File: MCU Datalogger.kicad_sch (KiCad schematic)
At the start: 25 parts, among them U1 24LC1025, U2 24LC1025, U3 ATMEGA328P-AU, U4 DS1337S_, Y1 Crystal, Y2 Crystal

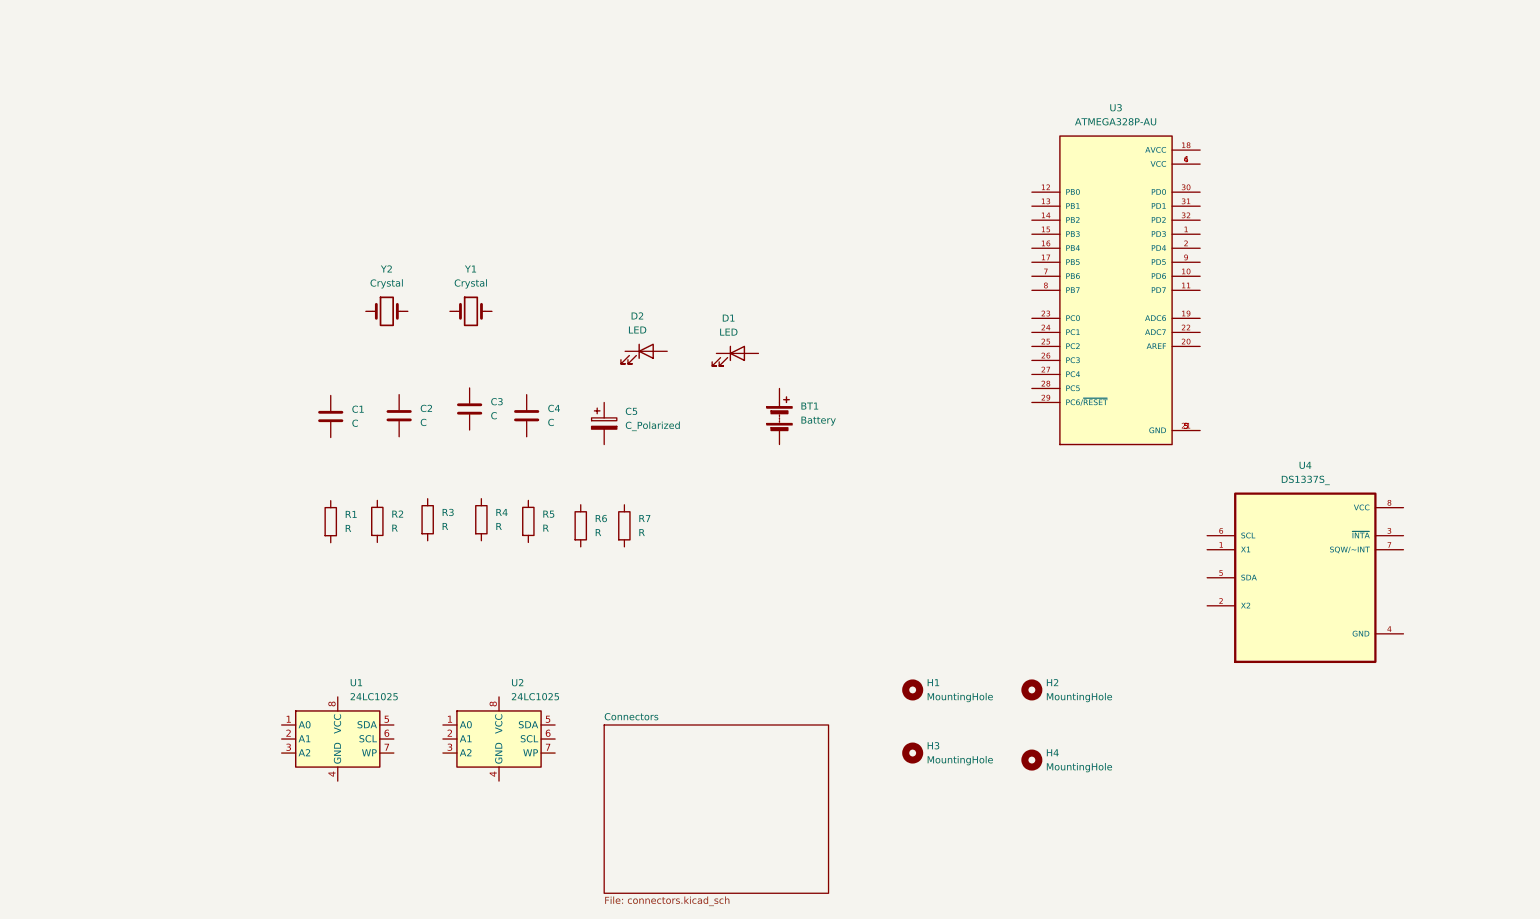
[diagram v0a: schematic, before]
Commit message: assigned footprint libraries
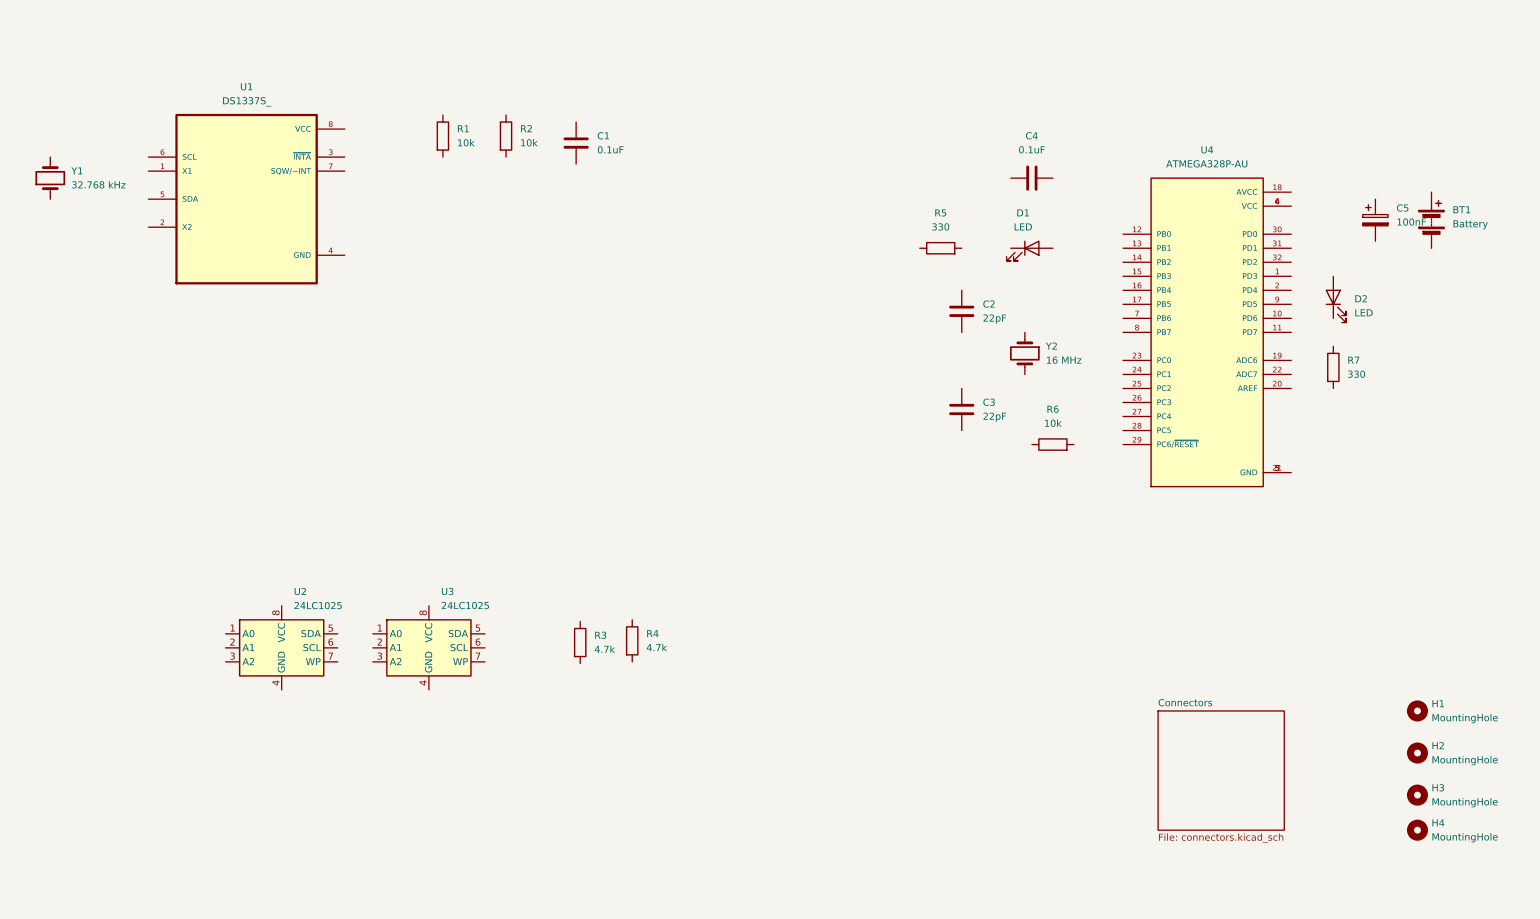
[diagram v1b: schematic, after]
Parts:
- removed U1: 24LC1025, symbol Memory_EEPROM:24LC1025
- removed U3: ATMEGA328P-AU, ATMEGA328P-AU:QFP80P900X900X120-32N, symbol ATMEGA328P-AU:ATMEGA328P-AU
- removed U4: DS1337S_, DS1337S_:SOIC127P600X175-8N, symbol DS1337S_:DS1337S_
- added U1: DS1337S_, footprints:SOIC127P600X175-8N, symbol DS1337S_:DS1337S_
- added U3: 24LC1025, Package_SO:SOIC-8_5.23x5.23mm_P1.27mm, symbol Memory_EEPROM:24LC1025
- added U4: ATMEGA328P-AU, footprints:QFP80P900X900X120-32N, symbol ATMEGA328P-AU:ATMEGA328P-AU
- BT1: footprint (none) -> Connector_PinHeader_2.54mm:PinHeader_1x02_P2.54mm_Vertical
- C1, C4: value C -> 0.1uF; footprint (none) -> Capacitor_SMD:C_0805_2012Metric
- C2, C3: value C -> 22pF; footprint (none) -> Capacitor_SMD:C_0805_2012Metric
- C5: value C_Polarized -> 100nF; footprint (none) -> Capacitor_SMD:C_0805_2012Metric
- D1, D2: footprint (none) -> LED_SMD:LED_0805_2012Metric
- H1, H2, H3, H4: footprint (none) -> MountingHole:MountingHole_2.1mm
- R1, R2, R6: value R -> 10k; footprint (none) -> Resistor_SMD:R_0805_2012Metric
- R3, R4: value R -> 4.7k; footprint (none) -> Resistor_SMD:R_0805_2012Metric
- R5, R7: value R -> 330; footprint (none) -> Resistor_SMD:R_0805_2012Metric
- U2: footprint (none) -> Package_SO:SOIC-8_5.23x5.23mm_P1.27mm
- Y1: value Crystal -> 32.768 kHz; footprint (none) -> Crystal:Crystal_SMD_5032-2Pin_5.0x3.2mm_HandSoldering
- Y2: value Crystal -> 16 MHz; footprint (none) -> Crystal:Crystal_SMD_5032-2Pin_5.0x3.2mm_HandSoldering
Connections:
- new net: U4.21 (GND), U4.3 (GND), U4.5 (GND)
- new net: U4.4 (VCC), U4.6 (VCC)
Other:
- company: (none) -> Artem Kostenko
- title: (none) -> ${project_name}

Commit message: wirred the 1st sheet
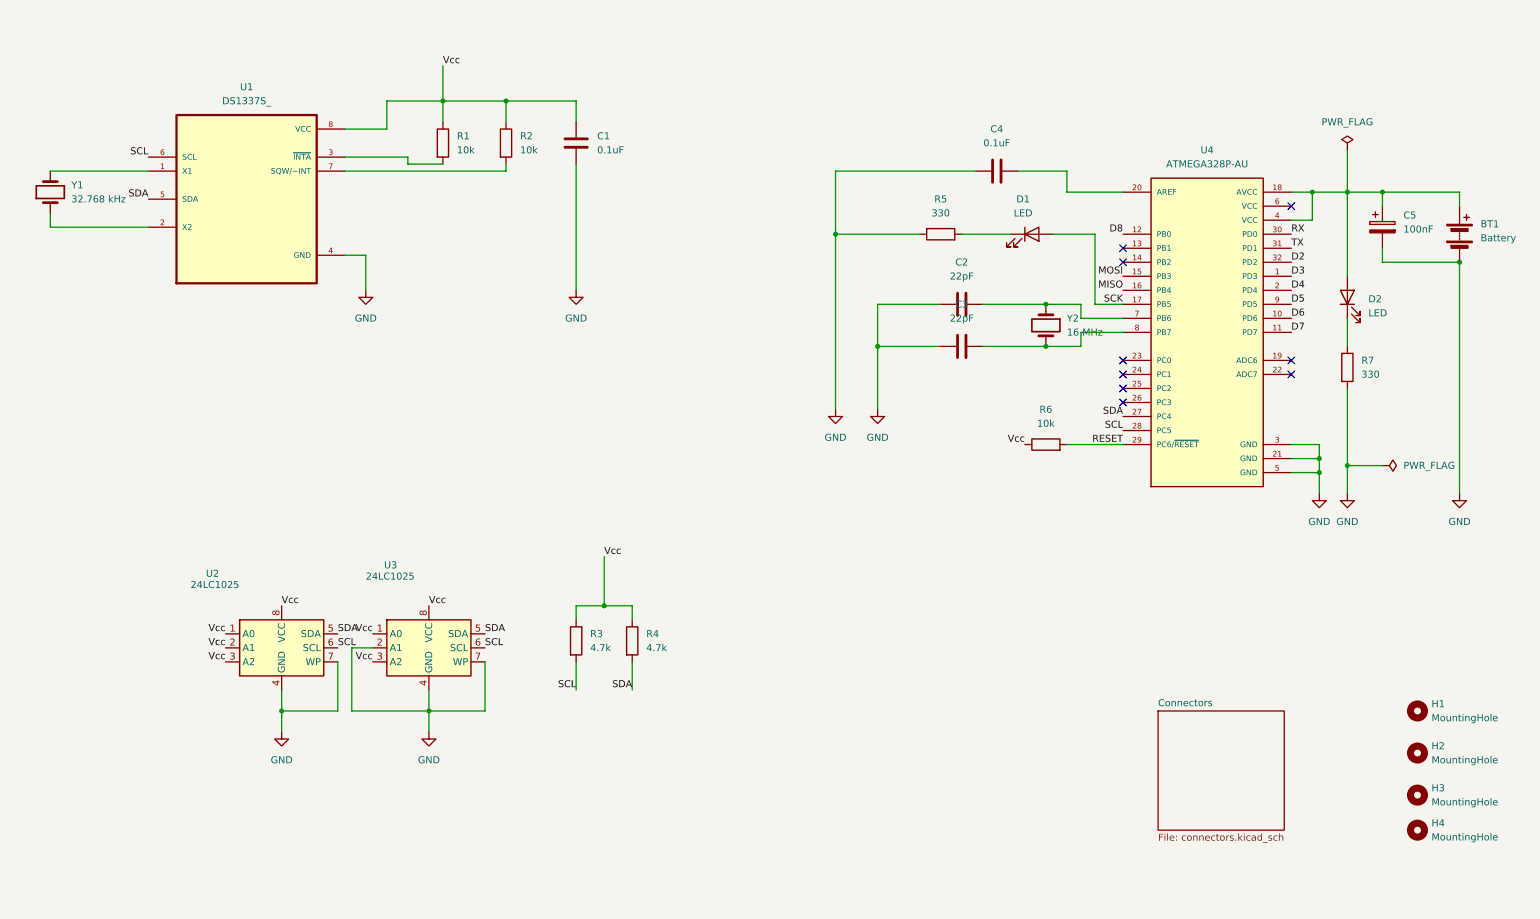
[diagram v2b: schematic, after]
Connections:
- net at C5.1: now also BT1.1 (+), D2.2 (A), U4.18 (AVCC), U4.4 (VCC)
- net GND: now reaches C5.2
- net GND: now also BT1.2 (-), C1.2, C2.1, C3.1, C4.1, R5.1, R7.2, U1.4 (GND), U2.4 (GND), U2.7 (WP), U3.2 (A1), U3.4 (GND), U3.7 (WP), U4.21 (GND), U4.3 (GND), U4.5 (GND)
- net at C3.2: now also U4.8 (PB7), Y2.2
- net at C4.2: now also U4.20 (AREF)
- net Vcc: now reaches R2.1
- net Vcc: now also C1.1, R1.1, R3.1, R4.1, R6.1, U1.8 (VCC), U2.1 (A0), U2.2 (A1), U2.3 (A2), U2.8 (VCC), U3.1 (A0), U3.3 (A2), U3.8 (VCC)
- net at R2.2: now also U1.7 (SQW/~INT)
- net SDA: now reaches R4.2
- net SDA: now also U1.5 (SDA), U2.5 (SDA), U3.5 (SDA), U4.27 (PC4)
- net SCL: now reaches U2.6 (SCL)
- net SCL: now also R3.2, U1.6 (SCL), U3.6 (SCL), U4.28 (PC5)
- net at Y1.1: now also U1.2 (X2)
- net at Y1.2: now also U1.1 (X1)
- net at U1.3 (~{INTA}): now also R1.2
- net at R7.1: now also D2.1 (K)
- net RESET: now reaches R6.2
- net RESET: now also U4.29 (PC6/~{RESET})
- net D3: now reaches U4.1 (PD3)
- net D6: now reaches U4.10 (PD6)
- net D7: now reaches U4.11 (PD7)
- net D8: now reaches U4.12 (PB0)
- net MOSI: now reaches U4.15 (PB3)
- net MISO: now reaches U4.16 (PB4)
- net SCK: now reaches U4.17 (PB5)
- net SCK: now also D1.2 (A)
- net D4: now reaches U4.2 (PD4)
- net RX: now reaches U4.30 (PD0)
- net TX: now reaches U4.31 (PD1)
- net D2: now reaches U4.32 (PD2)
- net at U4.6 (VCC): no longer U4.4 (VCC)
- net at U4.7 (PB6): now also C2.2, Y2.1
- net D5: now reaches U4.9 (PD5)
- net at D1.1 (K): now also R5.2
- no-connect marks 0 -> 9
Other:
- moved on the sheet: BT1, C2, C3, C4, C5, D1, D2, R1, R2, R3, R5, R6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

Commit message: finished project
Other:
- sheet Connectors ports: added D2, D3, D4, D5, D6, D7, D8, GND, MISO, MOSI, RESET, RX, SCL, SDA, TX, Vcc; removed none
- note added: "EEPROM"
- note added: "MCU"
- note added: "Mounting"
- note added: "Real time clock"
- moved on the sheet: H1, H2, H3, H4
